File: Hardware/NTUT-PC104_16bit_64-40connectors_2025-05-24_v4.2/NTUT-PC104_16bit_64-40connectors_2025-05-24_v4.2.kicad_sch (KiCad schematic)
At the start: 41 parts, among them J10 Conn_02x26_Odd_Even, J12 Conn_02x04_Odd_Even, J13 Conn_02x04_Odd_Even, J14 Conn_02x04_Odd_Even, J15 Conn_02x04_Odd_Even, J16 Conn_02x04_Odd_Even, J17 Conn_02x04_Odd_Even, J18 Conn_02x04_Odd_Even, J7 Conn_02x04_Odd_Even, J8 Conn_02x26_Odd_Even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

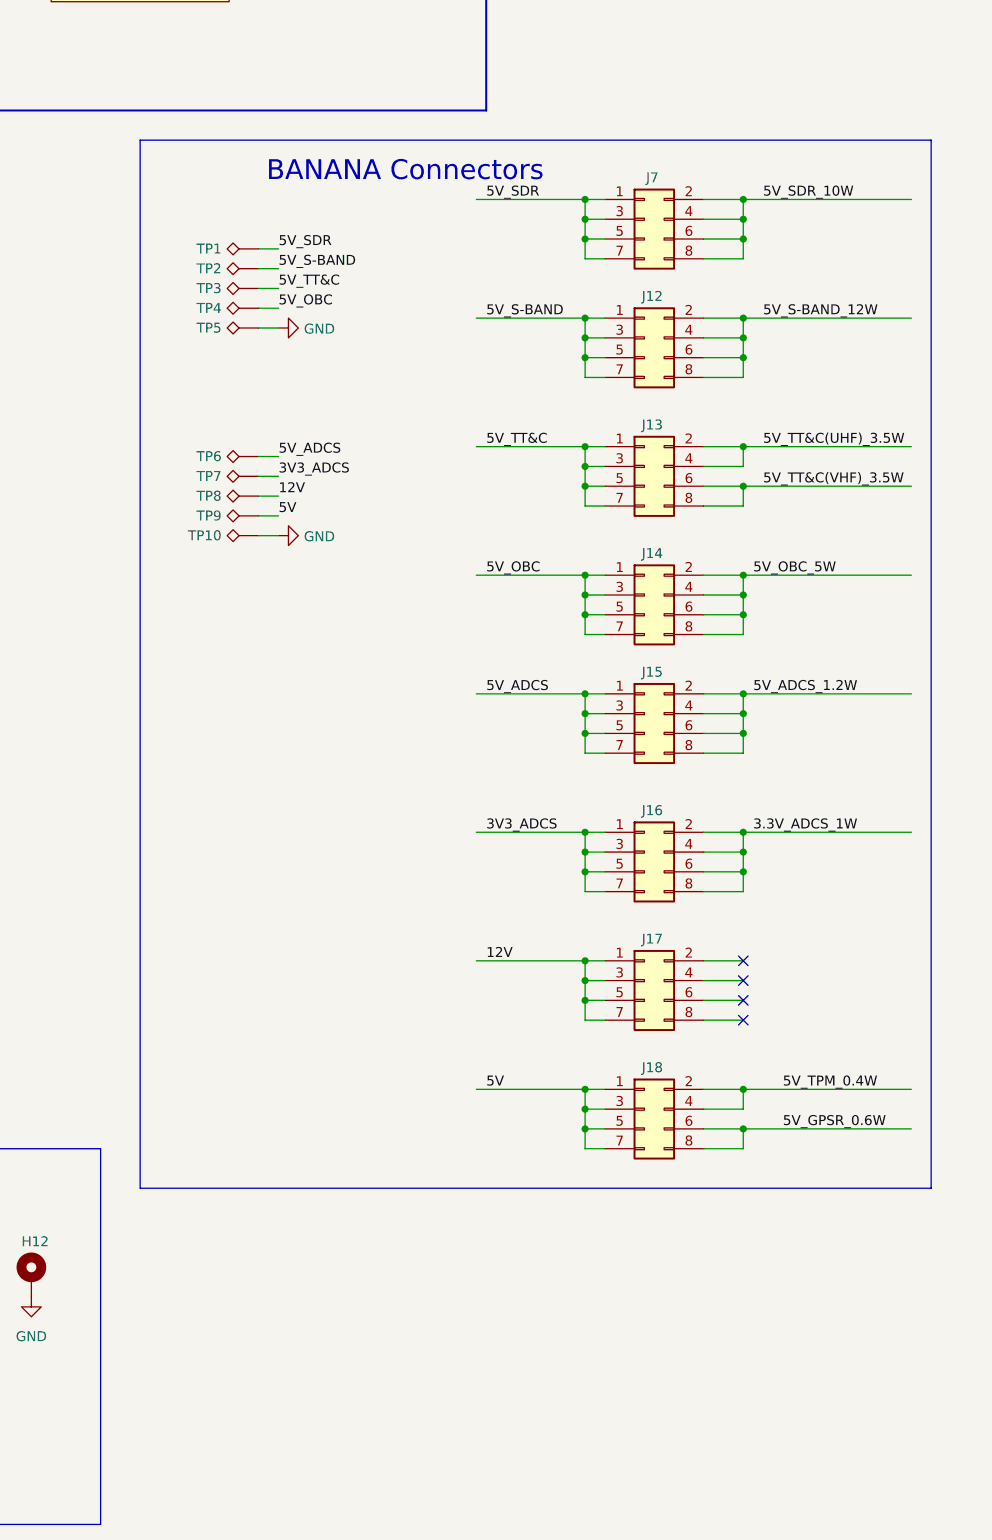
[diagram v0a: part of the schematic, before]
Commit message: 1. In NTUT-PC104_16bit_64-40connectors_2025-05-24_v4.2, reroute    5V_OBC_5W.
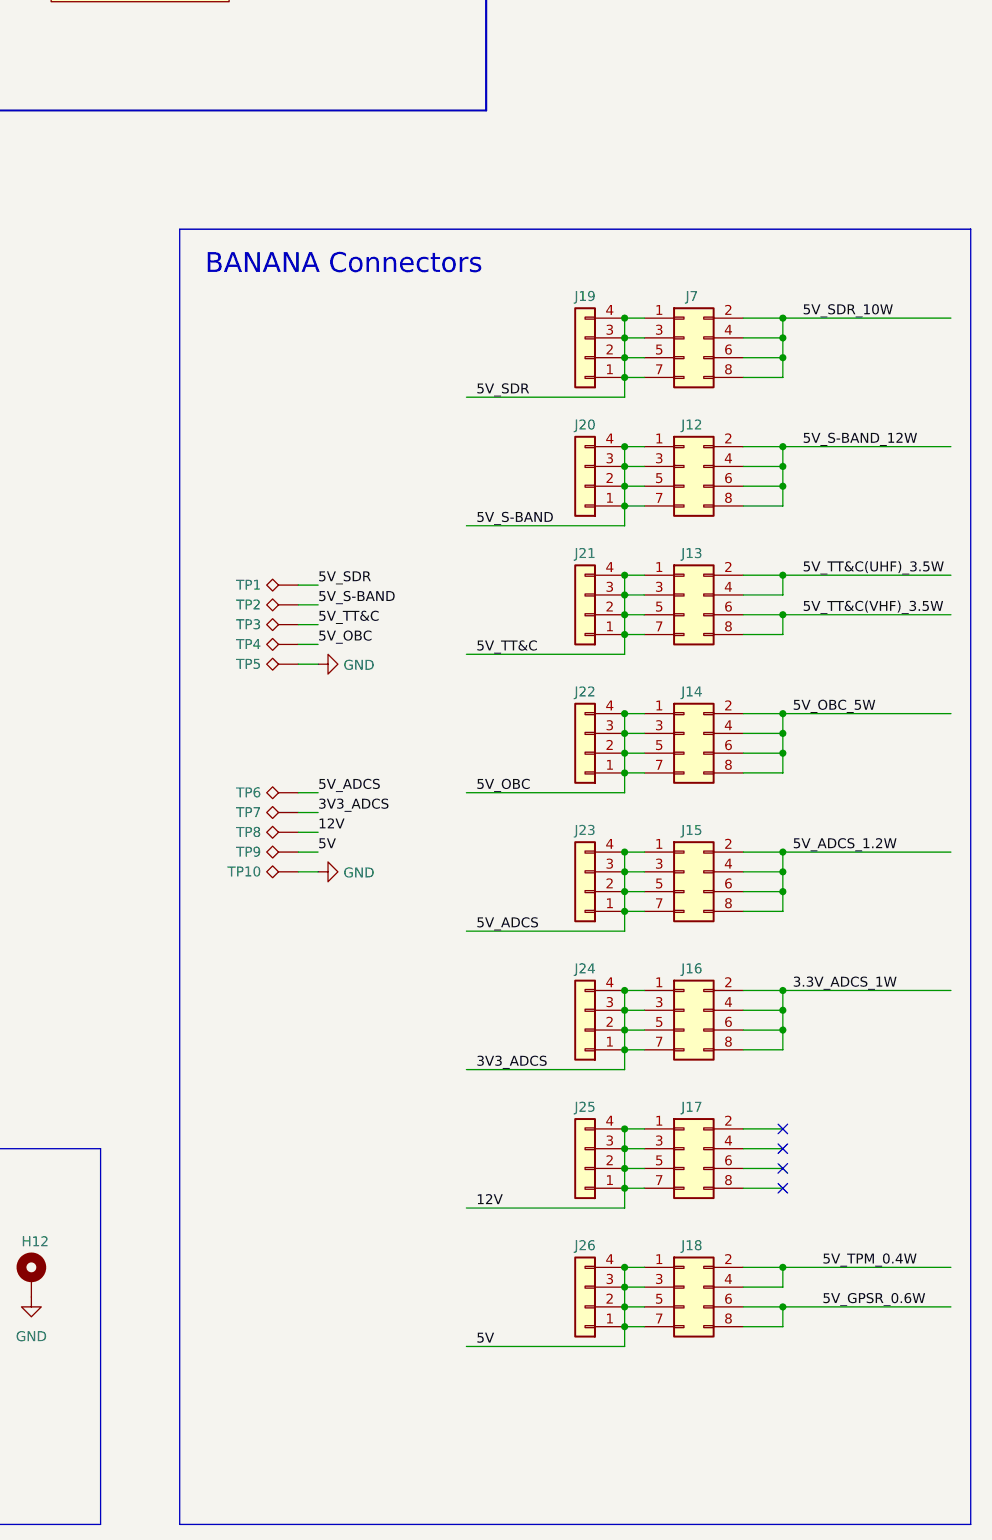
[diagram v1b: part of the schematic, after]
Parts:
- added J19, J20, J21, J22, J23, J24, J25, J26: Conn_01x04, Connector_PinHeader_2.54mm:PinHeader_1x04_P2.54mm_Vertical, symbol Connector_Generic:Conn_01x04
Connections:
- net 12V: now also J25.1 (Pin_1), J25.2 (Pin_2), J25.3 (Pin_3), J25.4 (Pin_4)
- net 3V3_ADCS: now also J24.1 (Pin_1), J24.2 (Pin_2), J24.3 (Pin_3), J24.4 (Pin_4)
- net 5V: now also J26.1 (Pin_1), J26.2 (Pin_2), J26.3 (Pin_3), J26.4 (Pin_4)
- net 5V_ADCS: now also J23.1 (Pin_1), J23.2 (Pin_2), J23.3 (Pin_3), J23.4 (Pin_4)
- net 5V_OBC: now also J22.1 (Pin_1), J22.2 (Pin_2), J22.3 (Pin_3), J22.4 (Pin_4)
- net 5V_S-BAND: now also J20.1 (Pin_1), J20.2 (Pin_2), J20.3 (Pin_3), J20.4 (Pin_4)
- net 5V_SDR: now also J19.1 (Pin_1), J19.2 (Pin_2), J19.3 (Pin_3), J19.4 (Pin_4)
- net 5V_TT&C: now also J21.1 (Pin_1), J21.2 (Pin_2), J21.3 (Pin_3), J21.4 (Pin_4)
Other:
- moved on the sheet: J12, J13, J14, J15, J16, J17, J18, J7, TP1, TP10, TP2, TP3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
